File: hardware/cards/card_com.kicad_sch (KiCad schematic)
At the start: 18 parts, among them J1 DE9_Pins, J2 Conn_01x03, J3 Conn_01x04, U1 16550, U2 MAX3241, U3 74HCT04, U4 74HCT08, U5 74HCT08, U6 74HCT125

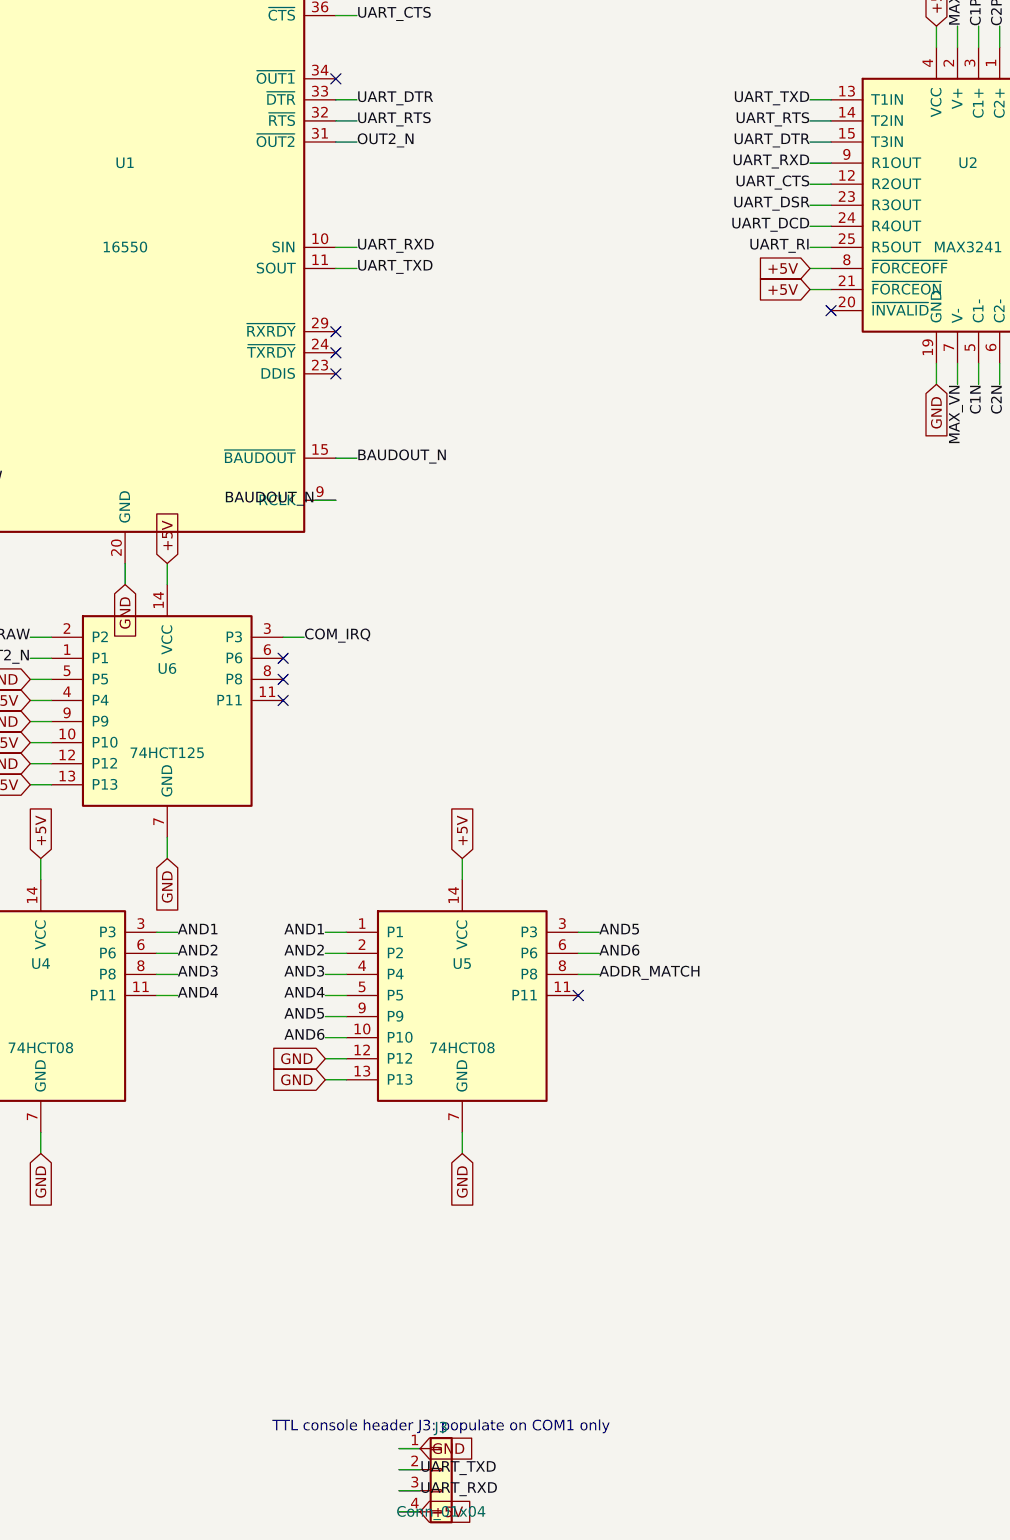
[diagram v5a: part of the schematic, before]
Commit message: Fix all medium design-review findings (M1-M8)
- M1: Supervisor link moved to GPIO4/5 (real UART1 pair); POST -> GPIO6-15
- M2: CNT_RUN = LD0.LD1.LD2 gates every '163 CEP (load-cascade hazard)
- M3: ~WR / IO-M pruned to cpu_core-internal; DRQ2/3 pulled + noted;
  doc S5.2 "as built: 48/48" + S16 updated
- M4: true XT-IDE rev-2 map (A0<->A3 swap): data 0x300, latch 0x301,
  CS1 0x307/0x30F, drive DA0 = bus A3 - matches XTIDE UB "rev 2" type
- M5: COM4 -> bus IRQ2 line (IRQ9 via AT redirect); IRQ10/11/14/15 marked
  off-header; ~REFRESH added to mxbus ISA_CTRL; questions-sidecar superseded
- M6: card_isatest clock tree on unswitched V5RAW (spec S8)
- M7: card_isatest IRQ2-8/DRQ1-3 idle pull-downs (spec S4/S9)
- M8: com_port JP1 selects 16550 RX source (DB9 vs TTL console); 5V note

Rebuilt motherboard + cards; structural ERC = 0; netlist-verified.
Fix log in hardware/notes/design-review-2026-07-03.md (batch 3).

Co-Authored-By: Claude Fable 5 <noreply@anthropic.com>
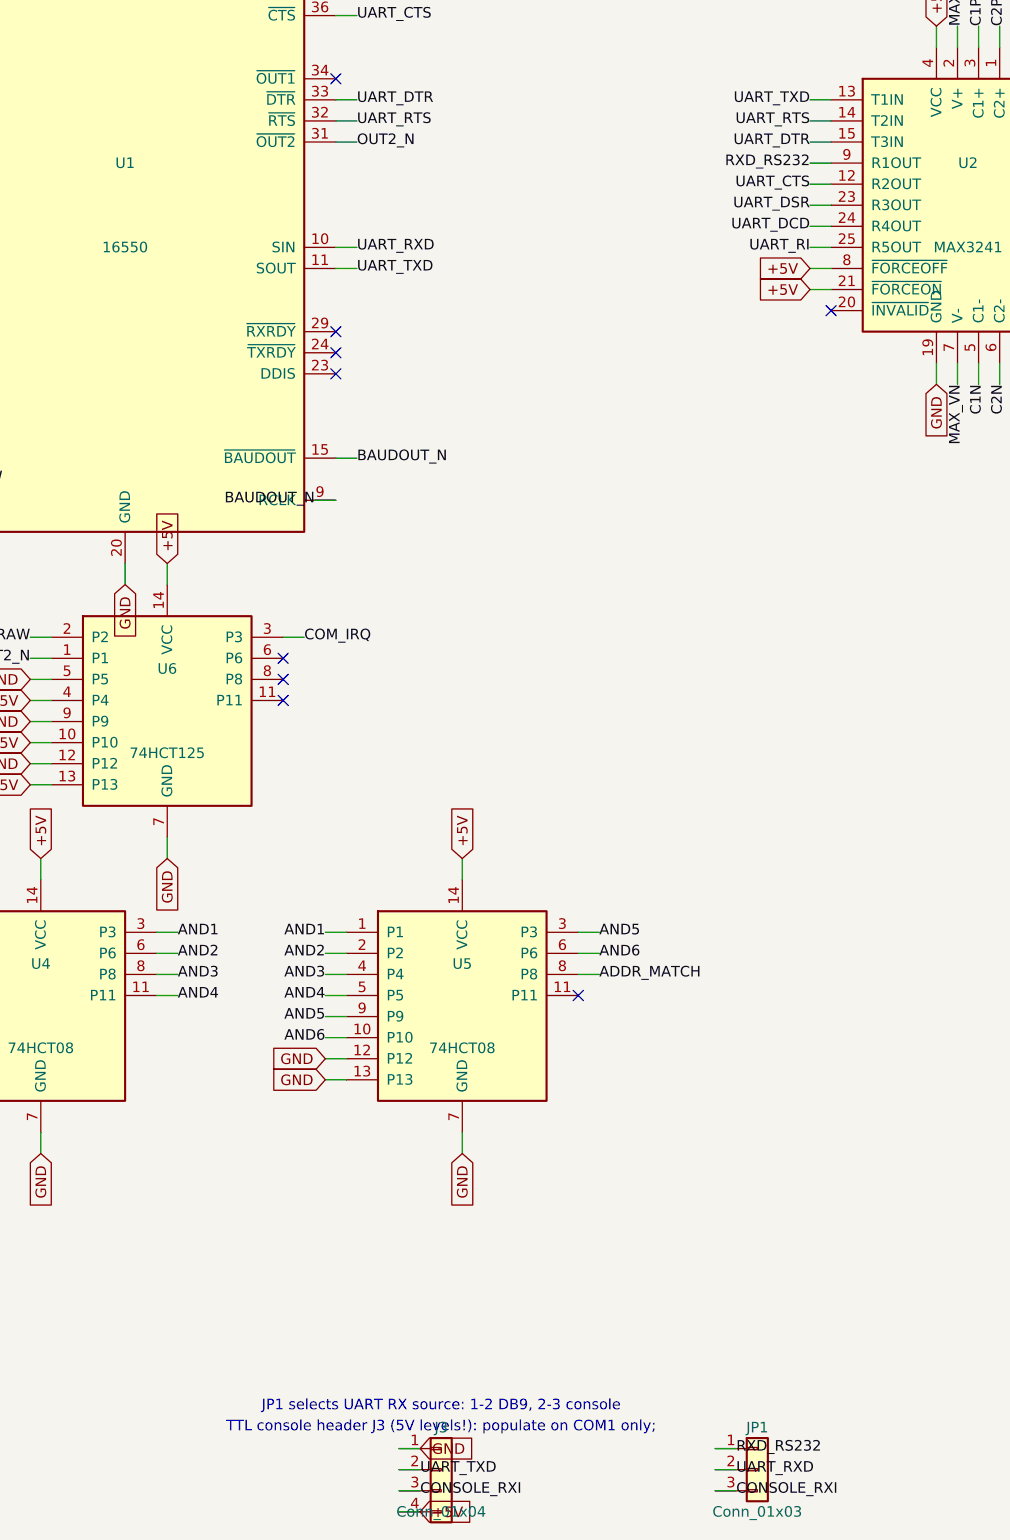
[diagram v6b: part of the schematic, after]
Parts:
- added JP1: Conn_01x03, symbol Connector_Generic:Conn_01x03
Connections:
- net UART_RXD: now also JP1.2 (Pin_2); no longer J3.3 (Pin_3), U2.9 (R1OUT)
- new net CONSOLE_RXI: J3.3 (Pin_3), JP1.3 (Pin_3)
- new net RXD_RS232: JP1.1 (Pin_1), U2.9 (R1OUT)
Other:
- note added: "JP1 selects UART RX source: 1-2 DB9, 2-3 console"
- note added: "TTL console header J3 (5V levels!): populate on COM1 only;"
- note removed: "TTL console header J3: populate on COM1 only"
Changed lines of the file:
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@@
 		)
 	)
-	(label "UART_RXD"
+	(label "RXD_RS232"
 		(at 209.55 96.52 180)
 		(effects
@@
 		)
 	)
-	(label "UART_RXD"
+	(label "CONSOLE_RXI"
 		(at 162.56 256.54 0)
 		(effects
@@
 	(wire
 		(pts
+			(xy 198.12 251.46)
+			(xy 200.66 251.46)
+		)
+		(stroke
+			(width 0)
+			(type default)
+		)
+	)
+	(label "RXD_RS232"
+		(at 200.66 251.46 0)
+		(effects
+			(font
+				(size 1.27 1.27)
+			)
+		)
+	)
+	(wire
+		(pts
+			(xy 198.12 254)
+			(xy 200.66 254)
+		)
+		(stroke
+			(width 0)
+			(type default)
+		)
+	)
+	(label "UART_RXD"
+		(at 200.66 254 0)
+		(effects
+			(font
+				(size 1.27 1.27)
+			)
+		)
+	)
+	(wire
+		(pts
+			(xy 198.12 256.54)
+			(xy 200.66 256.54)
+		)
+		(stroke
+			(width 0)
+			(type default)
+		)
+	)
+	(label "CONSOLE_RXI"
+		(at 200.66 256.54 0)
+		(effects
+			(font
+				(size 1.27 1.27)
+			)
+		)
+	)
+	(wire
+		(pts
 			(xy 109.22 46.99)
 			(xy 109.22 44.45)
@@
 		)
 	)
-	(text "TTL console header J3: populate on COM1 only"
+	(text "TTL console header J3 (5V levels!): populate on COM1 only;"
 		(at 165.1 248.92 0)
+		(effects
+			(font
+				(size 1.27 1.27)
+			)
+		)
+	)
+	(text "JP1 selects UART RX source: 1-2 DB9, 2-3 console"
+		(at 165.1 246.38 0)
 		(effects
 			(font
@@
 		(instances
 			(project "card_com"
-				(path "/4ecec349-12bf-42f6-a5d3-2a5fa6ecd768"
+				(path "/8e331aaf-16ef-483a-a762-d55a97b0571e"
 					(reference "J_IN")
 					(unit 1)
@@
 		(instances
 			(project "card_com"
-				(path "/4ecec349-12bf-42f6-a5d3-2a5fa6ecd768"
+				(path "/8e331aaf-16ef-483a-a762-d55a97b0571e"
 					(reference "J_OUT")
 					(unit 1)
@@
 		(instances
 			(project "card_com"
-				(path "/4ecec349-12bf-42f6-a5d3-2a5fa6ecd768"
+				(path "/8e331aaf-16ef-483a-a762-d55a97b0571e"
 					(reference "U1")
 					(unit 1)
@@
 		(instances
 			(project "card_com"
-				(path "/4ecec349-12bf-42f6-a5d3-2a5fa6ecd768"
+				(path "/8e331aaf-16ef-483a-a762-d55a97b0571e"
 					(reference "OSC1")
 					(unit 1)
@@
 		(instances
 			(project "card_com"
-				(path "/4ecec349-12bf-42f6-a5d3-2a5fa6ecd768"
+				(path "/8e331aaf-16ef-483a-a762-d55a97b0571e"
 					(reference "U3")
 					(unit 1)
@@
 		(instances
 			(project "card_com"
-				(path "/4ecec349-12bf-42f6-a5d3-2a5fa6ecd768"
+				(path "/8e331aaf-16ef-483a-a762-d55a97b0571e"
 					(reference "J2")
 					(unit 1)
@@
 		(instances
 			(project "card_com"
-				(path "/4ecec349-12bf-42f6-a5d3-2a5fa6ecd768"
+				(path "/8e331aaf-16ef-483a-a762-d55a97b0571e"
 					(reference "U4")
 					(unit 1)
@@
 		(instances
 			(project "card_com"
-				(path "/4ecec349-12bf-42f6-a5d3-2a5fa6ecd768"
+				(path "/8e331aaf-16ef-483a-a762-d55a97b0571e"
 					(reference "U5")
 					(unit 1)
@@
 		(instances
 			(project "card_com"
-				(path "/4ecec349-12bf-42f6-a5d3-2a5fa6ecd768"
+				(path "/8e331aaf-16ef-483a-a762-d55a97b0571e"
 					(reference "U6")
 					(unit 1)
@@
 		(instances
 			(project "card_com"
-				(path "/4ecec349-12bf-42f6-a5d3-2a5fa6ecd768"
+				(path "/8e331aaf-16ef-483a-a762-d55a97b0571e"
 					(reference "U2")
 					(unit 1)
@@
 		(instances
 			(project "card_com"
-				(path "/4ecec349-12bf-42f6-a5d3-2a5fa6ecd768"
+				(path "/8e331aaf-16ef-483a-a762-d55a97b0571e"
 					(reference "C3")
 					(unit 1)
@@
 		(instances
 			(project "card_com"
-				(path "/4ecec349-12bf-42f6-a5d3-2a5fa6ecd768"
+				(path "/8e331aaf-16ef-483a-a762-d55a97b0571e"
 					(reference "C4")
 					(unit 1)
@@
 		(instances
 			(project "card_com"
-				(path "/4ecec349-12bf-42f6-a5d3-2a5fa6ecd768"
+				(path "/8e331aaf-16ef-483a-a762-d55a97b0571e"
 					(reference "C5")
 					(unit 1)
@@
 		(instances
 			(project "card_com"
-				(path "/4ecec349-12bf-42f6-a5d3-2a5fa6ecd768"
+				(path "/8e331aaf-16ef-483a-a762-d55a97b0571e"
 					(reference "C6")
 					(unit 1)
@@
 		(instances
 			(project "card_com"
-				(path "/4ecec349-12bf-42f6-a5d3-2a5fa6ecd768"
+				(path "/8e331aaf-16ef-483a-a762-d55a97b0571e"
 					(reference "J1")
 					(unit 1)
@@
 		(instances
 			(project "card_com"
-				(path "/4ecec349-12bf-42f6-a5d3-2a5fa6ecd768"
+				(path "/8e331aaf-16ef-483a-a762-d55a97b0571e"
 					(reference "J3")
+					(unit 1)
+				)
+			)
+		)
+	)
+	(symbol
+		(lib_id "Connector_Generic:Conn_01x03")
+		(at 203.2 254 0)
+		(unit 1)
+		(exclude_from_sim no)
+		(in_bom yes)
+		(on_board yes)
+		(dnp no)
+		(fields_autoplaced yes)
+		(property "Reference" "JP1"
+			(at 203.2 248.92 0)
+			(effects
+				(font
+					(size 1.27 1.27)
+				)
+			)
+		)
+		(property "Value" "Conn_01x03"
+			(at 203.2 259.08 0)
+			(effects
+				(font
+					(size 1.27 1.27)
+				)
+			)
+		)
+		(property "Footprint" ""
+			(at 203.2 254 0)
+			(effects
+				(font
+					(size 1.27 1.27)
+				)
+				(hide yes)
+			)
+		)
+		(pin "1"
+		)
+		(pin "2"
+		)
+		(pin "3"
+		)
+		(instances
+			(project "card_com"
+				(path "/8e331aaf-16ef-483a-a762-d55a97b0571e"
+					(reference "JP1")
 					(unit 1)
 				)
@@
 		(instances
 			(project "card_com"
-				(path "/4ecec349-12bf-42f6-a5d3-2a5fa6ecd768"
+				(path "/8e331aaf-16ef-483a-a762-d55a97b0571e"
 					(reference "C1")
 					(unit 1)
@@
 		(instances
 			(project "card_com"
-				(path "/4ecec349-12bf-42f6-a5d3-2a5fa6ecd768"
+				(path "/8e331aaf-16ef-483a-a762-d55a97b0571e"
 					(reference "C2")
 					(unit 1)

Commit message: Fix all low-severity + toolchain design-review findings
Low:
- LPT IRQ7 via tri-state '125 (NAND-enabled ack pulse) - shareable line
- card_com JP2 IRQ strap follows the base-address strap (was IRQ4-only)
- Supervisor USB-A VBUS fused (500mA polyfuse)
- card_isatest: DUT_PWR_EN moved to the control '595 (addr shifts can't
  glitch DUT power); '165s -> 74HC grade (HCT needs VCC 4.5-5.5V)
- /3 duty comments corrected; U13 marked load-bearing inverting buffer
- RTC AS hold-path bench note; duplicate ~RD stub removed
- mxbus PRIV_DECODE emptied (Y5 never leaves cpu_core)

Toolchain:
- build.py/build_cards return real exit codes, failing on structural ERC
  (endpoint_off_grid/unconnected_wire_endpoint/multiple_net_names) or a
  failed netlist export
- KiCad paths resolved via mxsch.kicad_cli()/kicad_symdir() (env, PATH,
  snap `current`) - no pinned snap revision anywhere
- Deterministic UUIDs (uuid5 title-seed + counter): rebuilds are
  byte-identical (verified); this rewrites every UUID once
- S-expression string escapes now round-trip (parse decodes, dump encodes)
- CLAUDE.md updated to match

The new structural gate immediately caught its own batch's bug (pull row
placed inside card_isatest's J2 pin field) - moved and re-verified.

Co-Authored-By: Claude Fable 5 <noreply@anthropic.com>
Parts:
- added JP2: IRQ strap, symbol Connector_Generic:Conn_01x03
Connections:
- net COM_IRQ: now also JP2.2 (Pin_2); no longer J_IN.45 (Pin_45), J_OUT.45 (Pin_45)
- net IRQ3: now also JP2.3 (Pin_3)
- new net IRQ4: JP2.1 (Pin_1), J_IN.45 (Pin_45), J_OUT.45 (Pin_45)
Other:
- note added: "JP2: 1-2 = IRQ4 (strap J2 to 0x3F8/COM1), 2-3 = IRQ3 (0x2F8/COM2)"
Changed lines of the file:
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@@
 		)
 	)
-	(label "COM_IRQ"
+	(label "IRQ4"
 		(at 436.88 172.72 180)
 		(effects
@@
 		)
 	)
-	(label "COM_IRQ"
+	(label "IRQ4"
 		(at 500.38 172.72 180)
 		(effects
@@
 		)
 	)
+	(wire
+		(pts
+			(xy 414.02 149.86)
+			(xy 416.56 149.86)
+		)
+		(stroke
+			(width 0)
+			(type default)
+		)
+	)
+	(label "IRQ4"
+		(at 416.56 149.86 0)
+		(effects
+			(font
+				(size 1.27 1.27)
+			)
+		)
+	)
+	(wire
+		(pts
+			(xy 414.02 152.4)
+			(xy 416.56 152.4)
+		)
+		(stroke
+			(width 0)
+			(type default)
+		)
+	)
+	(label "COM_IRQ"
+		(at 416.56 152.4 0)
+		(effects
+			(font
+				(size 1.27 1.27)
+			)
+		)
+	)
+	(wire
+		(pts
+			(xy 414.02 154.94)
+			(xy 416.56 154.94)
+		)
+		(stroke
+			(width 0)
+			(type default)
+		)
+	)
+	(label "IRQ3"
+		(at 416.56 154.94 0)
+		(effects
+			(font
+				(size 1.27 1.27)
+			)
+		)
+	)
 	(text "Standalone Serial (COM) PCB: ISA bus chains J_IN -> J_OUT; card logic taps the bus by name. Daisy-chain cards header-to-header (isa_conn, S4.3)."
 		(at 38.1 12.7 0)
@@
 		)
 	)
+	(text "JP2: 1-2 = IRQ4 (strap J2 to 0x3F8/COM1), 2-3 = IRQ3 (0x2F8/COM2)"
+		(at 38.1 17.78 0)
+		(effects
+			(font
+				(size 1.27 1.27)
+			)
+		)
+	)
 	(symbol
 		(lib_id "Connector_Generic:Conn_02x30_Odd_Even")
@@
 		(instances
 			(project "card_com"
-				(path "/8e331aaf-16ef-483a-a762-d55a97b0571e"
+				(path "/4636acb9-3a64-5eff-8cec-9e5f72ae854d"
 					(reference "J_IN")
 					(unit 1)
@@
 		(instances
 			(project "card_com"
-				(path "/8e331aaf-16ef-483a-a762-d55a97b0571e"
+				(path "/4636acb9-3a64-5eff-8cec-9e5f72ae854d"
 					(reference "J_OUT")
 					(unit 1)
@@
 		(instances
 			(project "card_com"
-				(path "/8e331aaf-16ef-483a-a762-d55a97b0571e"
+				(path "/4636acb9-3a64-5eff-8cec-9e5f72ae854d"
 					(reference "U1")
 					(unit 1)
@@
 		(instances
 			(project "card_com"
-				(path "/8e331aaf-16ef-483a-a762-d55a97b0571e"
+				(path "/4636acb9-3a64-5eff-8cec-9e5f72ae854d"
 					(reference "OSC1")
 					(unit 1)
@@
 		(instances
 			(project "card_com"
-				(path "/8e331aaf-16ef-483a-a762-d55a97b0571e"
+				(path "/4636acb9-3a64-5eff-8cec-9e5f72ae854d"
 					(reference "U3")
 					(unit 1)
@@
 		(instances
 			(project "card_com"
-				(path "/8e331aaf-16ef-483a-a762-d55a97b0571e"
+				(path "/4636acb9-3a64-5eff-8cec-9e5f72ae854d"
 					(reference "J2")
 					(unit 1)
@@
 		(instances
 			(project "card_com"
-				(path "/8e331aaf-16ef-483a-a762-d55a97b0571e"
+				(path "/4636acb9-3a64-5eff-8cec-9e5f72ae854d"
 					(reference "U4")
 					(unit 1)
@@
 		(instances
 			(project "card_com"
-				(path "/8e331aaf-16ef-483a-a762-d55a97b0571e"
+				(path "/4636acb9-3a64-5eff-8cec-9e5f72ae854d"
 					(reference "U5")
 					(unit 1)
@@
 		(instances
 			(project "card_com"
-				(path "/8e331aaf-16ef-483a-a762-d55a97b0571e"
+				(path "/4636acb9-3a64-5eff-8cec-9e5f72ae854d"
 					(reference "U6")
 					(unit 1)
@@
 		(instances
 			(project "card_com"
-				(path "/8e331aaf-16ef-483a-a762-d55a97b0571e"
+				(path "/4636acb9-3a64-5eff-8cec-9e5f72ae854d"
 					(reference "U2")
 					(unit 1)
@@
 		(instances
 			(project "card_com"
-				(path "/8e331aaf-16ef-483a-a762-d55a97b0571e"
+				(path "/4636acb9-3a64-5eff-8cec-9e5f72ae854d"
 					(reference "C3")
 					(unit 1)
@@
 		(instances
 			(project "card_com"
-				(path "/8e331aaf-16ef-483a-a762-d55a97b0571e"
+				(path "/4636acb9-3a64-5eff-8cec-9e5f72ae854d"
 					(reference "C4")
 					(unit 1)
@@
 		(instances
 			(project "card_com"
-				(path "/8e331aaf-16ef-483a-a762-d55a97b0571e"
+				(path "/4636acb9-3a64-5eff-8cec-9e5f72ae854d"
 					(reference "C5")
 					(unit 1)
@@
 		(instances
 			(project "card_com"
-				(path "/8e331aaf-16ef-483a-a762-d55a97b0571e"
+				(path "/4636acb9-3a64-5eff-8cec-9e5f72ae854d"
 					(reference "C6")
 					(unit 1)
@@
 		(instances
 			(project "card_com"
-				(path "/8e331aaf-16ef-483a-a762-d55a97b0571e"
+				(path "/4636acb9-3a64-5eff-8cec-9e5f72ae854d"
 					(reference "J1")
 					(unit 1)
@@
 		(instances
 			(project "card_com"
-				(path "/8e331aaf-16ef-483a-a762-d55a97b0571e"
+				(path "/4636acb9-3a64-5eff-8cec-9e5f72ae854d"
 					(reference "J3")
 					(unit 1)
@@
 		(instances
 			(project "card_com"
-				(path "/8e331aaf-16ef-483a-a762-d55a97b0571e"
+				(path "/4636acb9-3a64-5eff-8cec-9e5f72ae854d"
 					(reference "JP1")
 					(unit 1)
@@
 		(instances
 			(project "card_com"
-				(path "/8e331aaf-16ef-483a-a762-d55a97b0571e"
+				(path "/4636acb9-3a64-5eff-8cec-9e5f72ae854d"
 					(reference "C1")
 					(unit 1)
@@
 		(instances
 			(project "card_com"
-				(path "/8e331aaf-16ef-483a-a762-d55a97b0571e"
+				(path "/4636acb9-3a64-5eff-8cec-9e5f72ae854d"
 					(reference "C2")
 					(unit 1)
 				)
+			)
+		)
+	)
+	(symbol
+		(lib_id "Connector_Generic:Conn_01x03")
+		(at 419.1 152.4 0)
+		(unit 1)
+		(exclude_from_sim no)
+		(in_bom yes)
+		(on_board yes)
+		(dnp no)
+		(fields_autoplaced yes)
+		(property "Reference" "JP2"
+			(at 419.1 147.32 0)
+			(effects
+				(font
+					(size 1.27 1.27)
+				)
+			)
+		)
+		(property "Value" "IRQ strap"
+			(at 419.1 157.48 0)
+			(effects
+				(font
+					(size 1.27 1.27)
+				)
+			)
+		)
+		(property "Footprint" ""
+			(at 419.1 152.4 0)
+			(effects
+				(font
+					(size 1.27 1.27)
+				)
+				(hide yes)
+			)
+		)
+		(pin "1"
+		)
+		(pin "2"
+		)
+		(pin "3"
+		)
+		(instances
+			(project "card_com"
+				(path "/4636acb9-3a64-5eff-8cec-9e5f72ae854d"
+					(reference "JP2")
+					(unit 1)
+				)
